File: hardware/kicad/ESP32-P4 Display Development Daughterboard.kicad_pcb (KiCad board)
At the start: 2 copper layers, 85 x 80 mm, 0 parts

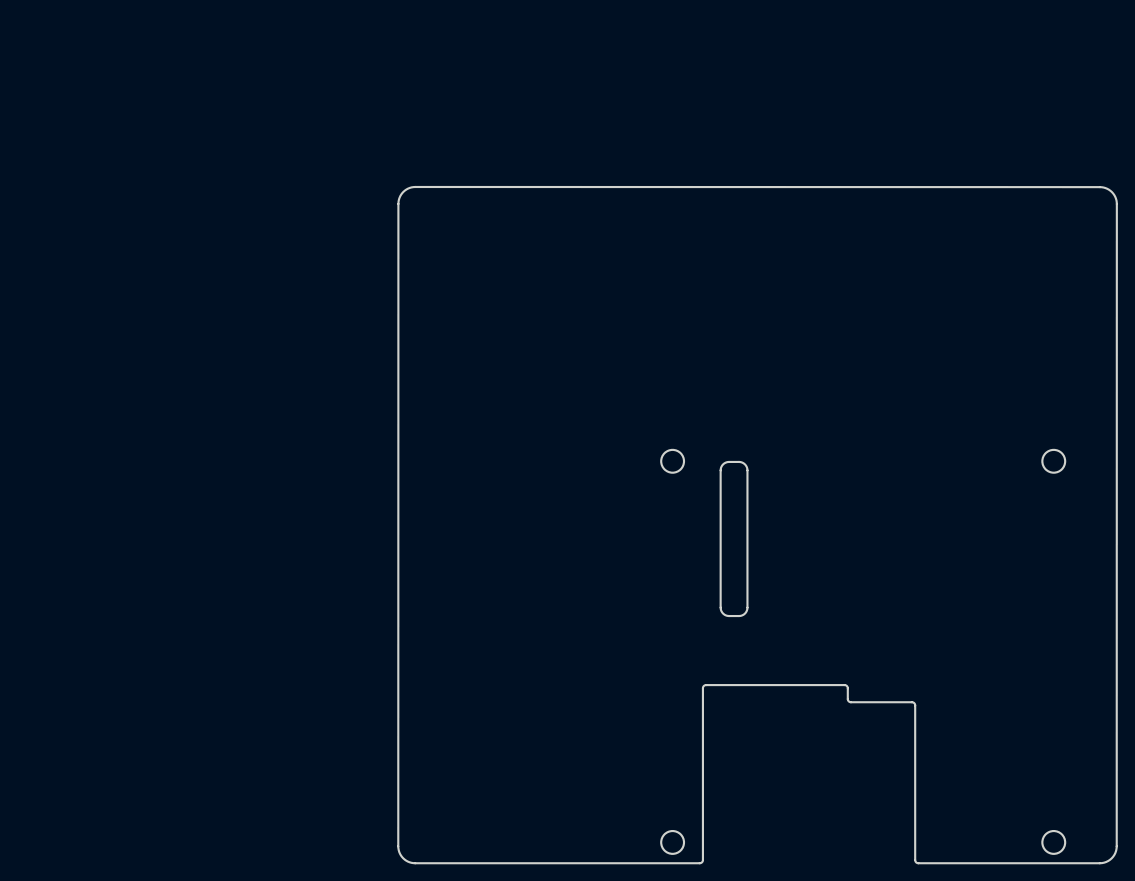
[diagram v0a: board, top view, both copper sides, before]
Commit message: Validate SSQ stack and add preliminary PCB placement
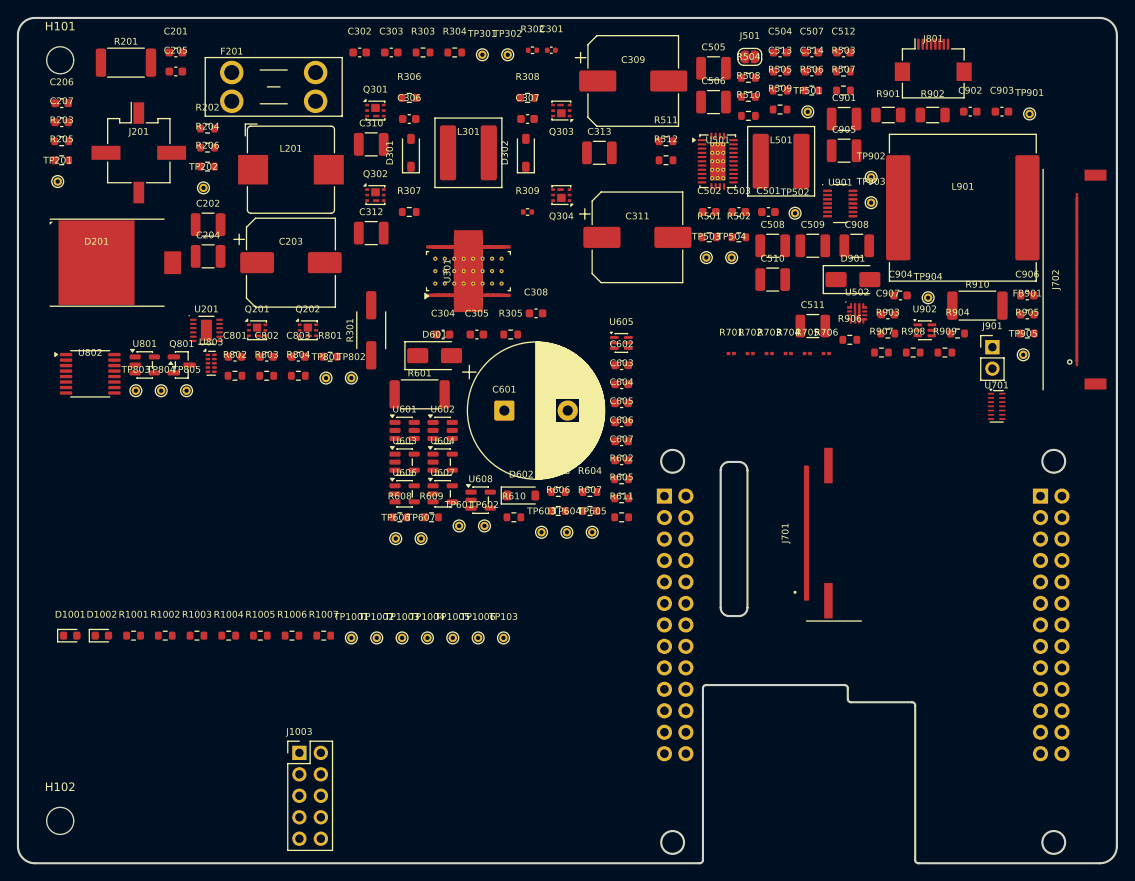
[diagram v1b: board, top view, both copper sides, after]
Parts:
- added C201: 100nF 100V, Capacitor_SMD:C_0603_1608Metric, F.Cu at (61.4, 28.1)
- added C202: 22uF 50V X7R, Capacitor_SMD:C_1210_3225Metric, F.Cu at (65.2, 48.5)
- added C203: 100uF 50V, Capacitor_SMD:CP_Elec_10x10, F.Cu at (75.0, 53.0)
- added C204: 10uF 50V, Capacitor_SMD:C_1210_3225Metric, F.Cu at (65.2, 52.2)
- added C205: 100nF 100V, Capacitor_SMD:C_0603_1608Metric, F.Cu at (61.4, 30.4)
- added C206: 100nF 100V, Capacitor_SMD:C_0603_1608Metric, F.Cu at (47.9, 34.1)
- added C207: 82nF 25V X7R, Capacitor_SMD:C_0603_1608Metric, F.Cu at (47.9, 36.4)
- added C301: 47pF C0G, Capacitor_SMD:C_0402_1005Metric, F.Cu at (105.8, 27.9)
- added C302: 270pF C0G, Capacitor_SMD:C_0603_1608Metric, F.Cu at (83.1, 28.1)
- added C303: 100nF, Capacitor_SMD:C_0603_1608Metric, F.Cu at (86.9, 28.1)
- added C304: 82nF X7R, Capacitor_SMD:C_0603_1608Metric, F.Cu at (93.0, 61.5)
- added C305: 270pF C0G, Capacitor_SMD:C_0603_1608Metric, F.Cu at (97.0, 61.5)
- added C306: 1uF 16V, Capacitor_SMD:C_0603_1608Metric, F.Cu at (89.0, 36.0)
- added C307: 100nF, Capacitor_SMD:C_0603_1608Metric, F.Cu at (103.0, 36.0)
- added C308: 100nF, Capacitor_SMD:C_0603_1608Metric, F.Cu at (104.0, 59.0)
- added C309: 220uF 35V, Capacitor_SMD:CP_Elec_10x12.5, F.Cu at (115.5, 31.5)
- added C310: 22uF 50V, Capacitor_SMD:C_1210_3225Metric, F.Cu at (84.5, 39.0)
- added C311: 220uF 35V, Capacitor_SMD:CP_Elec_10x12.5, F.Cu at (116.0, 50.0)
- added C312: 22uF 50V, Capacitor_SMD:C_1210_3225Metric, F.Cu at (84.5, 49.5)
- added C313: 22uF 50V, Capacitor_SMD:C_1210_3225Metric, F.Cu at (111.5, 40.0)
- added C501: 470nF, Capacitor_SMD:C_0603_1608Metric, F.Cu at (131.5, 47.0)
- added C502: 2.2uF 10V, Capacitor_SMD:C_0603_1608Metric, F.Cu at (124.5, 47.0)
- added C503: 1uF 10V, Capacitor_SMD:C_0603_1608Metric, F.Cu at (128.0, 47.0)
- added C504: 22nF, Capacitor_SMD:C_0603_1608Metric, F.Cu at (132.9, 28.1)
- added C505: 4.7uF 100V, Capacitor_SMD:C_1210_3225Metric, F.Cu at (125.0, 30.0)
- added C506: 4.7uF 100V, Capacitor_SMD:C_1210_3225Metric, F.Cu at (125.0, 34.0)
- added C507: 47nF 100V, Capacitor_SMD:C_0603_1608Metric, F.Cu at (136.6, 28.1)
- added C508: 22uF 10V, Capacitor_SMD:C_1210_3225Metric, F.Cu at (132.0, 51.0)
- added C509: 22uF 10V, Capacitor_SMD:C_1210_3225Metric, F.Cu at (136.8, 51.0)
- added C510: 22uF 10V, Capacitor_SMD:C_1210_3225Metric, F.Cu at (132.0, 55.0)
- added C511: 22uF 10V, Capacitor_SMD:C_1210_3225Metric, F.Cu at (136.8, 60.5)
- added C512: 10nF, Capacitor_SMD:C_0603_1608Metric, F.Cu at (140.4, 28.1)
- added C513: 1uF 10V, Capacitor_SMD:C_0603_1608Metric, F.Cu at (132.9, 30.4)
- added C514: 1uF 10V, Capacitor_SMD:C_0603_1608Metric, F.Cu at (136.6, 30.4)
- added C601: 6800uF 10V, Capacitor_THT:CP_Radial_D16.0mm_P7.50mm, F.Cu at (100.2, 70.5)
- added C602: 100pF C0G, Capacitor_SMD:C_0603_1608Metric, F.Cu at (114.1, 65.1)
- added C603: 1uF 10V, Capacitor_SMD:C_0603_1608Metric, F.Cu at (114.1, 67.4)
- added C604: 2.2uF 6.3V, Capacitor_SMD:C_0603_1608Metric, F.Cu at (114.1, 69.6)
- added C605: 2.2uF 6.3V, Capacitor_SMD:C_0603_1608Metric, F.Cu at (114.1, 71.9)
- added C606: 4.7uF 6.3V, Capacitor_SMD:C_0603_1608Metric, F.Cu at (114.1, 74.1)
- added C607: 1nF 50V C0G, Capacitor_SMD:C_0603_1608Metric, F.Cu at (114.1, 76.4)
- added C801: 1uF 10V, Capacitor_SMD:C_0603_1608Metric, F.Cu at (68.4, 64.1)
- added C802: 4.7uF 6.3V, Capacitor_SMD:C_0603_1608Metric, F.Cu at (72.1, 64.1)
- added C803: 100nF, Capacitor_SMD:C_0603_1608Metric, F.Cu at (75.9, 64.1)
- added C901: 10uF 50V, Capacitor_SMD:C_1210_3225Metric, F.Cu at (140.4, 36.0)
- added C902: 100nF 100V, Capacitor_SMD:C_0603_1608Metric, F.Cu at (155.4, 35.1)
- added C903: 1uF 10V, Capacitor_SMD:C_0603_1608Metric, F.Cu at (159.1, 35.1)
- added C904: 1nF 50V, Capacitor_SMD:C_0603_1608Metric, F.Cu at (147.1, 56.9)
- added C905: 2.2uF 50V, Capacitor_SMD:C_1210_3225Metric, F.Cu at (140.4, 39.8)
- added C906: 1nF, Capacitor_SMD:C_0603_1608Metric, F.Cu at (162.1, 56.9)
- added C907: 1nF, Capacitor_SMD:C_0603_1608Metric, F.Cu at (145.6, 59.1)
- added C908: 10uF 50V, Capacitor_SMD:C_1210_3225Metric, F.Cu at (141.9, 51.0)
- added D1001: GREEN, LED_SMD:LED_0603_1608Metric, F.Cu at (48.9, 97.1)
- added D1002: GREEN, LED_SMD:LED_0603_1608Metric, F.Cu at (52.6, 97.1)
- added D201: SM8S24CA-Q, Phase2:Bourns_DO-218AB, F.Cu at (52.0, 53.0)
- added D301: BAT46W-E3-08, Diode_SMD:D_SOD-123, F.Cu at (89.2, 40.0)
- added D302: BAT46W-E3-08, Diode_SMD:D_SOD-123, F.Cu at (102.8, 40.0)
- added D601: SS34-E3/57T, Diode_SMD:D_SMA, F.Cu at (92.0, 64.0)
- added D602: 1N4148W, Diode_SMD:D_SOD-123, F.Cu at (102.2, 80.5)
- added D901: SS2H10-E3/52T, Diode_SMD:D_SMA, F.Cu at (141.5, 55.0)
- added F201: 5A TIME DELAY, Fuse:Fuseholder_Blade_Mini_Keystone_3568, F.Cu at (68.0, 30.5)
- added FB901: 600R@100MHz 1A, Inductor_SMD:L_0603_1608Metric, F.Cu at (162.1, 59.1)
- added H101: M3 LEFT TOP SUPPORT, MountingHole:MountingHole_3.2mm_M3, F.Cu at (47.7, 29.1)
- added H102: M3 LEFT BOTTOM SUPPORT, MountingHole:MountingHole_3.2mm_M3, F.Cu at (47.7, 119.0)
- added J1001: SSQ-113-01-G-D, Phase2:Samtec_SSQ-113-01-G-D_BottomMount, B.Cu at (119.2, 80.6)
- added J1002: SSQ-113-01-G-D, Phase2:Samtec_SSQ-113-01-G-D_BottomMount, B.Cu at (163.7, 80.6)
- added J1003: DEBUG HEADER, Connector_PinHeader_2.54mm:PinHeader_2x05_P2.54mm_Vertical, F.Cu at (76.0, 111.0)
- added J201: VEHICLE 12V, Phase2:Molex_Micro-Fit_3.0_43045-0218_2x01-1MP_P3.00mm_Vertical, F.Cu at (57.0, 40.0)
- added J501: SERVICE LINK 5V, Jumper:SolderJumper-2_P1.3mm_Bridged_RoundedPad1.0x1.5mm, F.Cu at (129.3, 28.6)
- added J701: NANO DSI 15P, Phase2:Amphenol_SFW15R-2STE1LF, F.Cu at (136.0, 85.0)
- added J702: DISPLAYMAN LCD 40P, Phase2:Molex_505110-4096, F.Cu at (168.0, 55.0)
- added J801: GT9271 TOUCH 8P, Connector_FFC-FPC:Hirose_FH12-8S-0.5SH_1x08-1MP_P0.50mm_Horizontal, F.Cu at (151.0, 29.0)
- added J901: BL HARD DISABLE, Connector_PinHeader_2.54mm:PinHeader_1x02_P2.54mm_Vertical, F.Cu at (158.0, 63.0)
- added L201: 2.2uH 8A, Phase2:L_Bourns_SRP1038A_10.0x10.0mm, F.Cu at (75.0, 42.0)
- added L301: 15uH, Inductor_SMD:L_Coilcraft_XAL7070-XXX, F.Cu at (96.0, 40.0)
- added L501: 10uH, Inductor_SMD:L_Coilcraft_XAL7070-XXX, F.Cu at (133.0, 41.0)
- added L901: 68uH, Inductor_SMD:L_Vishay_IHLP-6767, F.Cu at (154.5, 46.5)
- added Q201: CSD19531Q5A, Package_SON:Texas_DQK, F.Cu at (71.0, 61.0)
- added Q202: CSD19531Q5A, Package_SON:Texas_DQK, F.Cu at (77.0, 61.0)
- added Q301: CSD19531Q5A, Package_SON:Texas_DQK, F.Cu at (85.0, 35.0)
- added Q302: CSD19531Q5A, Package_SON:Texas_DQK, F.Cu at (85.0, 45.0)
- added Q303: CSD19531Q5A, Package_SON:Texas_DQK, F.Cu at (107.0, 35.0)
- added Q304: CSD19531Q5A, Package_SON:Texas_DQK, F.Cu at (107.0, 45.0)
- added Q801: MMBT3904, Package_TO_SOT_SMD:SOT-23, F.Cu at (62.1, 65.1)
- added R1001: 100k, Resistor_SMD:R_0603_1608Metric, F.Cu at (56.4, 97.1)
- added R1002: 100k, Resistor_SMD:R_0603_1608Metric, F.Cu at (60.1, 97.1)
- added R1003: 100k, Resistor_SMD:R_0603_1608Metric, F.Cu at (63.9, 97.1)
- added R1004: 100k, Resistor_SMD:R_0603_1608Metric, F.Cu at (67.6, 97.1)
- added R1005: 47k, Resistor_SMD:R_0603_1608Metric, F.Cu at (71.4, 97.1)
- added R1006: 10k, Resistor_SMD:R_0603_1608Metric, F.Cu at (75.1, 97.1)
- added R1007: 2.2k, Resistor_SMD:R_0603_1608Metric, F.Cu at (78.9, 97.1)
- added R201: 1.0R 2W, Resistor_SMD:R_2512_6332Metric, F.Cu at (55.5, 29.3)
- added R202: 56.2k 1%, Resistor_SMD:R_0603_1608Metric, F.Cu at (65.1, 37.1)
- added R203: 10.0k 1%, Resistor_SMD:R_0603_1608Metric, F.Cu at (47.9, 38.6)
- added R204: 100k 1%, Resistor_SMD:R_0603_1608Metric, F.Cu at (65.1, 39.4)
- added R205: 6.49k 1%, Resistor_SMD:R_0603_1608Metric, F.Cu at (47.9, 40.9)
- added R206: 10.0k 1%, Resistor_SMD:R_0603_1608Metric, F.Cu at (65.1, 41.6)
- added R301: 20mR 1% 2W, Resistor_SMD:R_2512_6332Metric, F.Cu at (84.5, 61.0)
- added R302: 100R, Resistor_SMD:R_0402_1005Metric, F.Cu at (103.6, 27.9)
- added R303: 27.4k 1%, Resistor_SMD:R_0603_1608Metric, F.Cu at (90.6, 28.1)
- added R304: 93.1k 1%, Resistor_SMD:R_0603_1608Metric, F.Cu at (94.4, 28.1)
- added R305: 15.0k 1%, Resistor_SMD:R_0603_1608Metric, F.Cu at (101.0, 61.5)
- added R306: 580k 1%, Resistor_SMD:R_0603_1608Metric, F.Cu at (89.0, 33.5)
- added R307: 20.0k 1%, Resistor_SMD:R_0603_1608Metric, F.Cu at (89.0, 47.0)
- added R308: 47k, Resistor_SMD:R_0603_1608Metric, F.Cu at (103.0, 33.5)
- added R309: 100R, Resistor_SMD:R_0402_1005Metric, F.Cu at (103.0, 47.0)
- added R501: 100k 0.1%, Resistor_SMD:R_0603_1608Metric, F.Cu at (124.5, 50.0)
- added R502: 24.9k 0.1%, Resistor_SMD:R_0603_1608Metric, F.Cu at (128.0, 50.0)
- added R503: 1.00M 1%, Resistor_SMD:R_0603_1608Metric, F.Cu at (140.4, 30.4)
- added R504: 68.1k 1%, Resistor_SMD:R_0603_1608Metric, F.Cu at (129.1, 31.1)
- added R505: 549R 1%, Resistor_SMD:R_0603_1608Metric, F.Cu at (132.9, 32.6)
- added R506: 1.05k 1%, Resistor_SMD:R_0603_1608Metric, F.Cu at (136.6, 32.6)
- added R507: 100k, Resistor_SMD:R_0603_1608Metric, F.Cu at (140.4, 32.6)
- added R508: 26.7k, Resistor_SMD:R_0603_1608Metric, F.Cu at (129.1, 33.4)
- added R509: 47k, Resistor_SMD:R_0603_1608Metric, F.Cu at (132.9, 34.9)
- added R510: 47k, Resistor_SMD:R_0603_1608Metric, F.Cu at (129.1, 35.6)
- added R511: 100k, Resistor_SMD:R_0603_1608Metric, F.Cu at (119.4, 38.6)
- added R512: 100k, Resistor_SMD:R_0603_1608Metric, F.Cu at (119.4, 40.9)
- added R601: 3.3R 2W PULSE, Resistor_SMD:R_2512_6332Metric, F.Cu at (90.2, 68.6)
- added R602: 1.00M 1%, Resistor_SMD:R_0603_1608Metric, F.Cu at (114.1, 78.6)
- added R603: 21.5k 1%, Resistor_SMD:R_0603_1608Metric, F.Cu at (106.6, 80.1)
- added R604: 47k, Resistor_SMD:R_0603_1608Metric, F.Cu at (110.4, 80.1)
- added R605: 10k, Resistor_SMD:R_0603_1608Metric, F.Cu at (114.1, 80.9)
- added R606: 47k, Resistor_SMD:R_0603_1608Metric, F.Cu at (106.6, 82.4)
- added R607: 47k, Resistor_SMD:R_0603_1608Metric, F.Cu at (110.4, 82.4)
- added R608: 47k, Resistor_SMD:R_0603_1608Metric, F.Cu at (87.9, 83.1)
- added R609: 47k, Resistor_SMD:R_0603_1608Metric, F.Cu at (91.6, 83.1)
- added R610: 10k, Resistor_SMD:R_0603_1608Metric, F.Cu at (101.4, 83.1)
- added R611: 100k, Resistor_SMD:R_0603_1608Metric, F.Cu at (114.1, 83.1)
- added R701: 0R 0201, Resistor_SMD:R_0201_0603Metric, F.Cu at (127.1, 63.8)
- added R702: 0R 0201, Resistor_SMD:R_0201_0603Metric, F.Cu at (129.3, 63.8)
- added R703: 0R 0201, Resistor_SMD:R_0201_0603Metric, F.Cu at (131.6, 63.8)
- added R704: 0R 0201, Resistor_SMD:R_0201_0603Metric, F.Cu at (133.8, 63.8)
- added R705: 0R 0201, Resistor_SMD:R_0201_0603Metric, F.Cu at (136.1, 63.8)
- added R706: 0R 0201, Resistor_SMD:R_0201_0603Metric, F.Cu at (138.3, 63.8)
- added R801: 100k, Resistor_SMD:R_0603_1608Metric, F.Cu at (79.6, 64.1)
- added R802: 100k, Resistor_SMD:R_0603_1608Metric, F.Cu at (68.4, 66.4)
- added R803: 4.7k, Resistor_SMD:R_0603_1608Metric, F.Cu at (72.1, 66.4)
- added R804: 100k, Resistor_SMD:R_0603_1608Metric, F.Cu at (75.9, 66.4)
- added R901: 1.65R 0.1%, Resistor_SMD:R_1206_3216Metric, F.Cu at (145.7, 35.5)
- added R902: 1.65R 0.1%, Resistor_SMD:R_1206_3216Metric, F.Cu at (150.9, 35.5)
- added R903: 100R, Resistor_SMD:R_0603_1608Metric, F.Cu at (145.6, 61.4)
- added R904: 83k 1%, Resistor_SMD:R_0603_1608Metric, F.Cu at (153.9, 61.4)
- added R905: 100R, Resistor_SMD:R_0603_1608Metric, F.Cu at (162.1, 61.4)
- added R906: 0R, Resistor_SMD:R_0603_1608Metric, F.Cu at (141.1, 62.1)
- added R907: 1.00M, Resistor_SMD:R_0603_1608Metric, F.Cu at (144.9, 63.6)
- added R908: 47k, Resistor_SMD:R_0603_1608Metric, F.Cu at (148.6, 63.6)
- added R909: 100k, Resistor_SMD:R_0603_1608Metric, F.Cu at (152.4, 63.6)
- added R910: 0R LED CURRENT LINK, Resistor_SMD:R_2512_6332Metric, F.Cu at (156.2, 58.1)
- added TP1001: LCD_PWR_EN, TestPoint:TestPoint_THTPad_D1.0mm_Drill0.5mm, F.Cu at (82.2, 97.4)
- added TP1002: LCD_RESET_CMD_N, TestPoint:TestPoint_THTPad_D1.0mm_Drill0.5mm, F.Cu at (85.2, 97.4)
- added TP1003: BL_PWM, TestPoint:TestPoint_THTPad_D1.0mm_Drill0.5mm, F.Cu at (88.2, 97.4)
- added TP1004: CTP_RESET_N_NANO, TestPoint:TestPoint_THTPad_D1.0mm_Drill0.5mm, F.Cu at (91.2, 97.4)
- added TP1005: CTP_INT_NANO, TestPoint:TestPoint_THTPad_D1.0mm_Drill0.5mm, F.Cu at (94.2, 97.4)
- added TP1006: GND, TestPoint:TestPoint_THTPad_D1.0mm_Drill0.5mm, F.Cu at (97.2, 97.4)
- added TP103: GND, TestPoint:TestPoint_THTPad_D1.0mm_Drill0.5mm, F.Cu at (100.2, 97.4)
- added TP201: VEH_12V_RAW, TestPoint:TestPoint_THTPad_D1.0mm_Drill0.5mm, F.Cu at (47.4, 43.4)
- added TP202: VEH_PROT, TestPoint:TestPoint_THTPad_D1.0mm_Drill0.5mm, F.Cu at (64.7, 44.1)
- added TP301: SYS_24V, TestPoint:TestPoint_THTPad_D1.0mm_Drill0.5mm, F.Cu at (97.7, 28.4)
- added TP302: SYS24_PGOOD, TestPoint:TestPoint_THTPad_D1.0mm_Drill0.5mm, F.Cu at (100.7, 28.4)
- added TP501: SYS_5V_3A, TestPoint:TestPoint_THTPad_D1.0mm_Drill0.5mm, F.Cu at (136.2, 35.1)
- added TP502: NANO_5V, TestPoint:TestPoint_THTPad_D1.0mm_Drill0.5mm, F.Cu at (134.7, 47.1)
- added TP503: SYS5_PGOOD, TestPoint:TestPoint_THTPad_D1.0mm_Drill0.5mm, F.Cu at (124.2, 52.4)
- added TP504: NANO_EFUSE_FLT, TestPoint:TestPoint_THTPad_D1.0mm_Drill0.5mm, F.Cu at (127.2, 52.4)
- added TP601: VIN_GOOD, TestPoint:TestPoint_THTPad_D1.0mm_Drill0.5mm, F.Cu at (94.9, 84.2)
- added TP602: SEQ_FLAG1, TestPoint:TestPoint_THTPad_D1.0mm_Drill0.5mm, F.Cu at (97.9, 84.2)
- added TP603: SEQ_FLAG2, TestPoint:TestPoint_THTPad_D1.0mm_Drill0.5mm, F.Cu at (104.7, 84.9)
- added TP604: SEQ_FLAG3, TestPoint:TestPoint_THTPad_D1.0mm_Drill0.5mm, F.Cu at (107.7, 84.9)
- added TP605: LCD_IOVCC, TestPoint:TestPoint_THTPad_D1.0mm_Drill0.5mm, F.Cu at (110.7, 84.9)
- added TP606: LCD_VCI, TestPoint:TestPoint_THTPad_D1.0mm_Drill0.5mm, F.Cu at (87.4, 85.7)
- added TP607: LCD_RESET_N, TestPoint:TestPoint_THTPad_D1.0mm_Drill0.5mm, F.Cu at (90.4, 85.7)
- added TP801: TOUCH_3V3, TestPoint:TestPoint_THTPad_D1.0mm_Drill0.5mm, F.Cu at (79.2, 66.7)
- added TP802: CTP_SCL, TestPoint:TestPoint_THTPad_D1.0mm_Drill0.5mm, F.Cu at (82.2, 66.7)
- added TP803: CTP_SDA, TestPoint:TestPoint_THTPad_D1.0mm_Drill0.5mm, F.Cu at (56.6, 68.2)
- added TP804: CTP_INT, TestPoint:TestPoint_THTPad_D1.0mm_Drill0.5mm, F.Cu at (59.6, 68.2)
- added TP805: CTP_RESET_N, TestPoint:TestPoint_THTPad_D1.0mm_Drill0.5mm, F.Cu at (62.6, 68.2)
- added TP901: BL_PWM, TestPoint:TestPoint_THTPad_D1.0mm_Drill0.5mm, F.Cu at (162.4, 35.4)
- added TP902: BL_DIM, TestPoint:TestPoint_THTPad_D1.0mm_Drill0.5mm, F.Cu at (143.7, 42.9)
- added TP903: LED_A, TestPoint:TestPoint_THTPad_D1.0mm_Drill0.5mm, F.Cu at (143.7, 45.9)
- added TP904: LED_K, TestPoint:TestPoint_THTPad_D1.0mm_Drill0.5mm, F.Cu at (150.4, 57.1)
- added TP905: BL_FAULT_N, TestPoint:TestPoint_THTPad_D1.0mm_Drill0.5mm, F.Cu at (161.7, 63.9)
- added U201: LM74800QDRRRQ1, Phase2:Texas_DRR0012E_WSON-12_3x3mm_P0.5mm_EP1.3x2.5mm, F.Cu at (65.0, 61.0)
- added U301: LM5176QPWPRQ1, Phase2:Texas_PWP0028V_TSSOP-28-1EP_4.4x9.7mm_P0.65mm_EP3.4x9.7mm_Mask2.94x5.62mm_ThermalVias, F.Cu at (96.0, 54.0)
- added U501: LM76003RNPR, Phase2:Texas_RNP0030B_WQFN-30-1EP_4x6mm_P0.5mm_EP1.8x4.5mm_ThermalVias, F.Cu at (125.5, 41.0)
- added U502: TPS259470ARPWR, Phase2:Texas_RPW0010A_VQFN-HR-10_2x2mm, F.Cu at (142.0, 59.0)
- added U601: TPS3808G01DBVR, Package_TO_SOT_SMD:SOT-23-6, F.Cu at (88.5, 72.8)
- added U602: LM3880MF-1AA/NOPB, Package_TO_SOT_SMD:SOT-23-6, F.Cu at (93.0, 72.8)
- added U603: TLV75518PDBVR, Package_TO_SOT_SMD:SOT-23-5, F.Cu at (88.5, 76.6)
- added U604: TLV75528PDBVR, Package_TO_SOT_SMD:SOT-23-5, F.Cu at (93.0, 76.6)
- added U605: TPS22919DCKR, Package_TO_SOT_SMD:SOT-363_SC-70-6, F.Cu at (114.1, 62.5)
- added U606: SN74LVC1G07DBVR, Package_TO_SOT_SMD:SOT-23-5, F.Cu at (88.5, 80.3)
- added U607: SN74LVC1G07DBVR, Package_TO_SOT_SMD:SOT-23-5, F.Cu at (93.0, 80.3)
- added U608: SN74LVC1G07DBVR, Package_TO_SOT_SMD:SOT-23-5, F.Cu at (97.5, 81.1)
- added U701: TPD6E05U06RVZR, Package_SON:Texas_R-PUSON-N14, F.Cu at (158.5, 70.0)
- added U801: TLV75533PDBVR, Package_TO_SOT_SMD:SOT-23-5, F.Cu at (57.7, 65.1)
- added U802: TMUX1574PWR, Package_SO:TSSOP-16_4.4x5mm_P0.65mm, F.Cu at (51.2, 66.2)
- added U803: TPD4E05U06DQAR, Package_SON:USON-10_2.5x1.0mm_P0.5mm, F.Cu at (65.6, 64.9)
- added U901: TPS922053DYYR, Phase2:Texas_DYY0014A_TSOT-23-14, F.Cu at (140.0, 46.0)
- added U902: SN74LVC1G11DCKR, Package_TO_SOT_SMD:SOT-363_SC-70-6, F.Cu at (150.0, 61.0)
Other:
- board size 85 x 80 mm -> 130 x 100 mm

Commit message: Replace preliminary floorplan with routing-ready placement
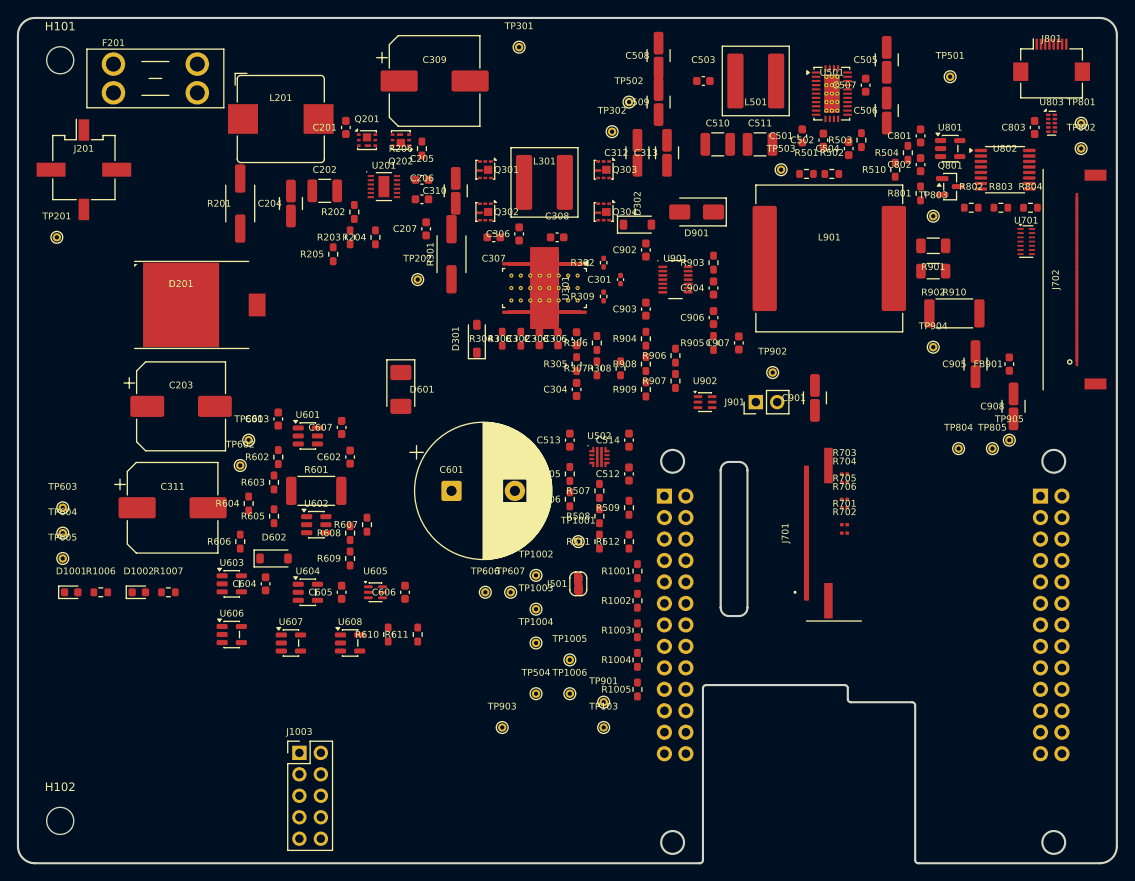
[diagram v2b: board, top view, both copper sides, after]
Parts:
- moved U802 110.9 mm to (159.5, 42.0)
- moved U803 103.4 mm to (165.0, 36.5)
- moved U801 98.7 mm to (153.0, 39.5)
- moved TP803 96.6 mm to (151.0, 47.5)
- moved TP805 95.6 mm to (158.0, 75.0)
- moved TP804 94.6 mm to (154.0, 75.0)
- moved TP801 94.3 mm to (168.5, 36.5)
- moved Q801 93.3 mm to (153.0, 44.0)
- moved C803 91.2 mm to (163.0, 37.0), turned to 90 degrees
- moved TP802 90.5 mm to (168.5, 39.5)
- moved R802 89.4 mm to (155.5, 46.5)
- moved R803 89.1 mm to (159.0, 46.5)
- moved R804 88.9 mm to (162.5, 46.5)
- moved TP901 85.9 mm to (112.0, 105.0)
- moved C801 85.2 mm to (149.5, 38.0), turned to 90 degrees
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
